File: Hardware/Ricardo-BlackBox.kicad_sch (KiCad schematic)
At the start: 45 parts, among them J1 RBUS, J3 Conn_01x08_Pin, U1 ESP32-S3, U7 LM66200DRLR, Y1 R940000171

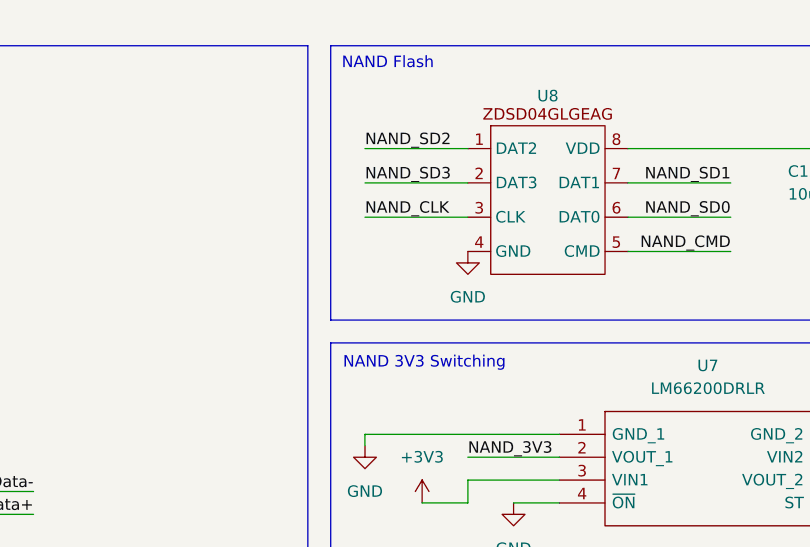
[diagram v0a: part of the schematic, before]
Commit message: Moved NAND flash chip and added debounce resistor
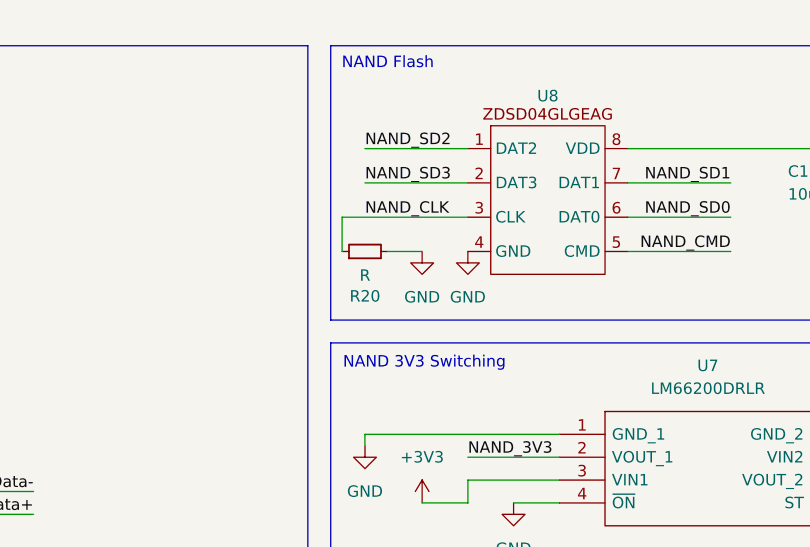
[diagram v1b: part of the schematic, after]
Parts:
- added R20: R, Resistor_SMD:R_0402_1005Metric, symbol Device:R_Small
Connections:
- net GND: now also R20.2
- net NAND_CLK: now also R20.1
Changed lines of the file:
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@@
 	(wire
 		(pts
-			(xy 181.61 31.75) (xy 193.04 31.75)
-		)
-		(stroke
-			(width 0)
-			(type default)
-		)
-	)
-	(wire
-		(pts
 			(xy 107.95 180.34) (xy 115.57 180.34)
 		)
@@
 	(wire
 		(pts
+			(xy 179.07 31.75) (xy 193.04 31.75)
+		)
+		(stroke
+			(width 0)
+			(type default)
+		)
+	)
+	(wire
+		(pts
 			(xy 55.88 165.1) (xy 63.5 165.1)
 		)
@@
 	(wire
 		(pts
+			(xy 184.15 35.56) (xy 187.96 35.56)
+		)
+		(stroke
+			(width 0)
+			(type default)
+		)
+	)
+	(wire
+		(pts
 			(xy 125.73 25.4) (xy 125.73 26.67)
 		)
@@
 	(wire
 		(pts
+			(xy 179.07 35.56) (xy 179.07 31.75)
+		)
+		(stroke
+			(width 0)
+			(type default)
+		)
+	)
+	(wire
+		(pts
 			(xy 34.29 170.18) (xy 34.29 165.1)
 		)
@@
 	)
 	(symbol
+		(lib_id "Device:R_Small")
+		(at 181.61 35.56 90)
+		(unit 1)
+		(exclude_from_sim no)
+		(in_bom yes)
+		(on_board yes)
+		(dnp no)
+		(property "Reference" "R20"
+			(at 181.61 40.5384 90)
+			(effects
+				(font
+					(size 1.27 1.27)
+				)
+			)
+		)
+		(property "Value" "R"
+			(at 181.61 38.227 90)
+			(effects
+				(font
+					(size 1.27 1.27)
+				)
+			)
+		)
+		(property "Footprint" "Resistor_SMD:R_0402_1005Metric"
+			(at 181.61 35.56 0)
+			(effects
+				(font
+					(size 1.27 1.27)
+				)
+				(hide yes)
+			)
+		)
+		(property "Datasheet" "~"
+			(at 181.61 35.56 0)
+			(effects
+				(font
+					(size 1.27 1.27)
+				)
+				(hide yes)
+			)
+		)
+		(property "Description" "Resistor, small symbol"
+			(at 181.61 35.56 0)
+			(effects
+				(font
+					(size 1.27 1.27)
+				)
+				(hide yes)
+			)
+		)
+		(pin "1"
+		)
+		(pin "2"
+		)
+		(instances
+			(project "Ricardo-BlackBox"
+				(path "/7db990e4-92e1-4f99-b4d2-435bbec1ba83"
+					(reference "R20")
+					(unit 1)
+				)
+			)
+		)
+	)
+	(symbol
 		(lib_id "Device:C_Small")
 		(at 20.32 138.43 0)
@@
 					(unit 1)
 				)
+			)
+		)
+	)
+	(symbol
+		(lib_id "power:GND")
+		(at 187.96 35.56 0)
+		(unit 1)
+		(exclude_from_sim no)
+		(in_bom yes)
+		(on_board yes)
+		(dnp no)
+		(fields_autoplaced yes)
+		(property "Reference" "#PWR056"
+			(at 187.96 41.91 0)
+			(effects
+				(font
+					(size 1.27 1.27)
+				)
+				(hide yes)
+			)
+		)
+		(property "Value" "GND"
+			(at 187.96 40.64 0)
+			(effects
+				(font
+					(size 1.27 1.27)
+				)
+			)
+		)
+		(property "Footprint" ""
+			(at 187.96 35.56 0)
+			(effects
+				(font
+					(size 1.27 1.27)
+				)
+				(hide yes)
+			)
+		)
+		(property "Datasheet" ""
+			(at 187.96 35.56 0)
+			(effects
+				(font
+					(size 1.27 1.27)
+				)
+				(hide yes)
+			)
+		)
+		(property "Description" "Power symbol creates a global label with name \"GND\" , ground"
+			(at 187.96 35.56 0)
+			(effects
+				(font
+					(size 1.27 1.27)
+				)
+				(hide yes)
+			)
+		)
+		(pin "1"
+		)
+		(instances
+			(project "Ricardo-BlackBox"
+				(path "/7db990e4-92e1-4f99-b4d2-435bbec1ba83"
+					(reference "#PWR056")
+					(unit 1)
+				)
